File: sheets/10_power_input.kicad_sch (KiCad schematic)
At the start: 8 parts, among them Q1 BUK9M35-80EX, U2 LM74700

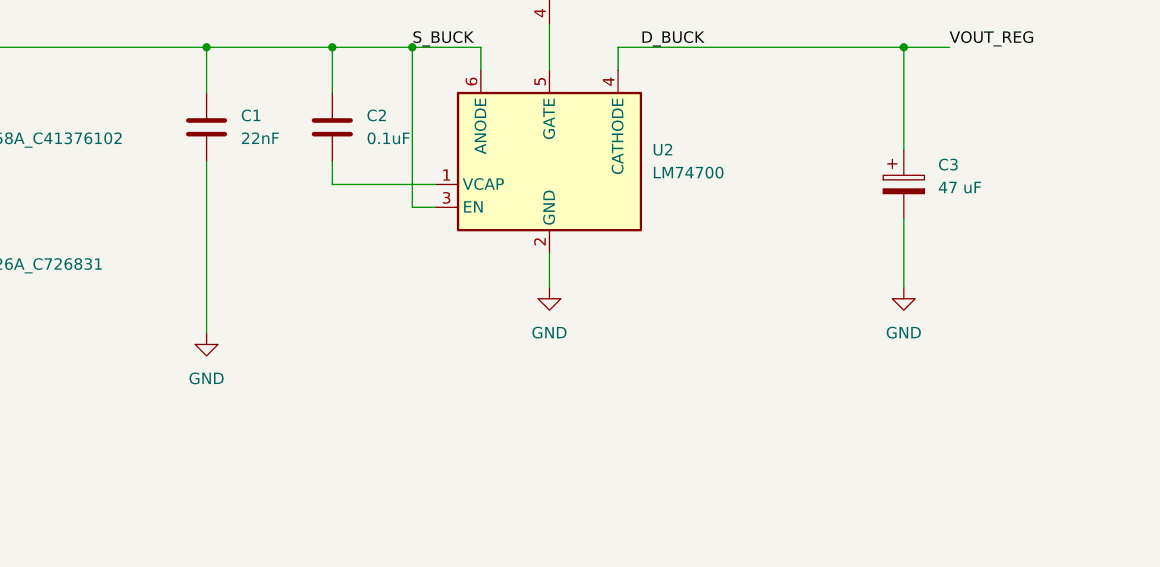
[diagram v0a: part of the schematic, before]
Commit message: Corrige la base del esquemático y añade reglas de proyecto
- Extrae el símbolo ADM3055E a lib/antmicro_adm3055ebriz.kicad_sym y lo
  registra en sym-lib-table con ${KIPRJMOD}.
- U1: huella Package_SO:SOIC-20W_7.5x12.8mm_P1.27mm (nota: verificar
  land pattern contra el datasheet).
- 10_power_input: power:GND -> GND_VEH; huellas y MPN de C1, C2 (0805
  X7R 100 V automotriz), C3 (EEE-HA2A470UP, 10x10) y F1 (1812, MPN
  pendiente).
- Nuevos pines jerárquicos CAN_SILENT (40_mcu -> 60_can, pull-down R1
  10k a GND_ISO) e IMU_INT2 (50_sensors -> 40_mcu).
- CLAUDE.md con reglas de librerías, campos, conexiones entre hojas,
  verificación por hoja y versión prototipo.
- Ignora output/ (reportes generados por kicad-mcp).

Co-Authored-By: Claude Opus 5.5 <noreply@anthropic.com>
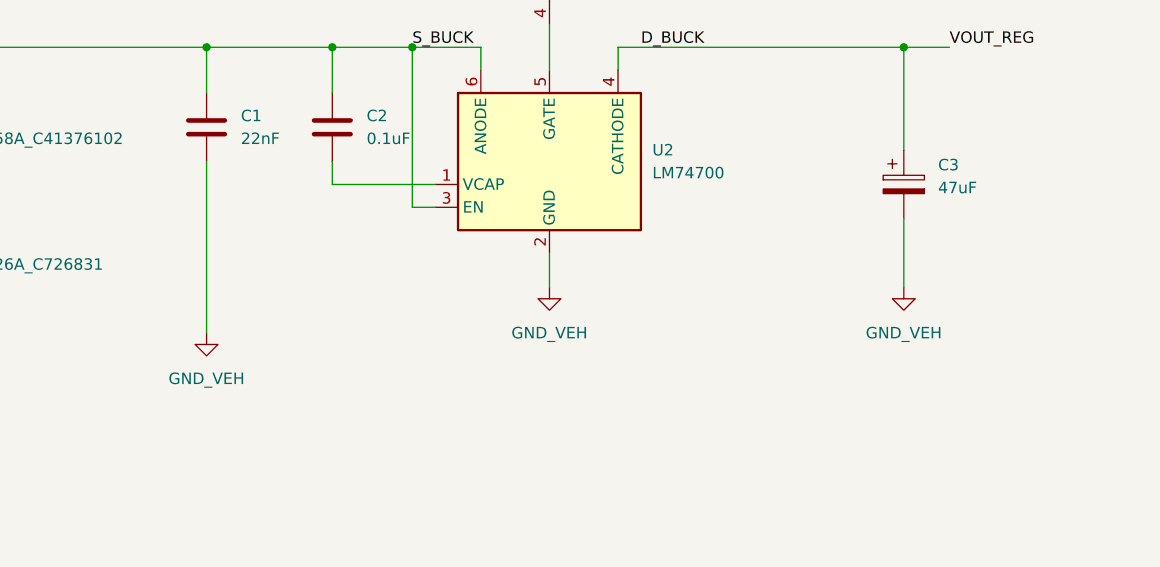
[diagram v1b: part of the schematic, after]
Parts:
- C1: footprint (none) -> Capacitor_SMD:C_0805_2012Metric; MPN (none) -> GCM21BR72A223KA37L; Manufacturer (none) -> Murata; Notes (none) -> 0805 en vez de 0603: lado vehicular (transitorios hasta ~94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; Rating (none) -> 100V X7R 0805 AEC-Q200
- C2: footprint (none) -> Capacitor_SMD:C_0805_2012Metric; MPN (none) -> CGA4J2X7R2A104K125AA; Manufacturer (none) -> TDK; Notes (none) -> 0805 en vez de 0603: lado vehicular (transitorios hasta ~94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; Rating (none) -> 100V X7R 0805 AEC-Q200
- C3: value 47 uF -> 47uF; footprint (none) -> Capacitor_SMD:CP_Elec_10x10; LCSC (none) -> C344077; MPN (none) -> EEE-HA2A470UP; Manufacturer (none) -> Panasonic; Rating (none) -> 100V 105C AEC-Q200 10x10.2
- F1: footprint (none) -> Fuse:Fuse_1812_4532Metric; MPN (none) -> TBD (I_hold pendiente); Manufacturer (none) -> TBD
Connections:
- net GND is gone; now on net GND_VEH: C1.2, C3.2, U2.2 (GND)
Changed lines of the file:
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@@
 			)
 		)
-		(property "Footprint" ""
+		(property "Footprint" "Capacitor_SMD:C_0805_2012Metric"
 			(at 202.8952 133.35 0)
 			(hide yes)
@@
 			)
 		)
-		(property "Datasheet" ""
+		(property "Datasheet" "https://product.tdk.com/en/search/capacitor/ceramic/mlcc/info?part_no=CGA4J2X7R2A104K125AA"
 			(at 201.93 129.54 0)
 			(hide yes)
@@
 		)
 		(property "Description" "Unpolarized capacitor"
+			(at 201.93 129.54 0)
+			(hide yes)
+			(show_name no)
+			(do_not_autoplace no)
+			(effects
+				(font
+					(size 1.27 1.27)
+				)
+			)
+		)
+		(property "MPN" "CGA4J2X7R2A104K125AA"
+			(at 201.93 129.54 0)
+			(hide yes)
+			(show_name no)
+			(do_not_autoplace no)
+			(effects
+				(font
+					(size 1.27 1.27)
+				)
+			)
+		)
+		(property "Manufacturer" "TDK"
+			(at 201.93 129.54 0)
+			(hide yes)
+			(show_name no)
+			(do_not_autoplace no)
+			(effects
+				(font
+					(size 1.27 1.27)
+				)
+			)
+		)
+		(property "Alt_MPN" ""
+			(at 201.93 129.54 0)
+			(hide yes)
+			(show_name no)
+			(do_not_autoplace no)
+			(effects
+				(font
+					(size 1.27 1.27)
+				)
+			)
+		)
+		(property "Rating" "100V X7R 0805 AEC-Q200"
+			(at 201.93 129.54 0)
+			(hide yes)
+			(show_name no)
+			(do_not_autoplace no)
+			(effects
+				(font
+					(size 1.27 1.27)
+				)
+			)
+		)
+		(property "Notes" "0805 en vez de 0603: lado vehicular (transitorios hasta ~94 V tras D1), menor perdida por DC bias que 0603 a 100 V y mas robusto a flexion cerca del conector"
 			(at 201.93 129.54 0)
 			(hide yes)
@@
 			)
 		)
-		(property "Footprint" ""
+		(property "Footprint" "Capacitor_SMD:C_0805_2012Metric"
 			(at 188.9252 133.35 0)
 			(hide yes)
@@
 			)
 		)
-		(property "Datasheet" ""
+		(property "Datasheet" "https://www.murata.com/en-us/products/productdetail?partno=GCM21BR72A223KA37%23"
 			(at 187.96 129.54 0)
 			(hide yes)
@@
 		)
 		(property "Description" "Unpolarized capacitor"
+			(at 187.96 129.54 0)
+			(hide yes)
+			(show_name no)
+			(do_not_autoplace no)
+			(effects
+				(font
+					(size 1.27 1.27)
+				)
+			)
+		)
+		(property "MPN" "GCM21BR72A223KA37L"
+			(at 187.96 129.54 0)
+			(hide yes)
+			(show_name no)
+			(do_not_autoplace no)
+			(effects
+				(font
+					(size 1.27 1.27)
+				)
+			)
+		)
+		(property "Manufacturer" "Murata"
+			(at 187.96 129.54 0)
+			(hide yes)
+			(show_name no)
+			(do_not_autoplace no)
+			(effects
+				(font
+					(size 1.27 1.27)
+				)
+			)
+		)
+		(property "Alt_MPN" ""
+			(at 187.96 129.54 0)
+			(hide yes)
+			(show_name no)
+			(do_not_autoplace no)
+			(effects
+				(font
+					(size 1.27 1.27)
+				)
+			)
+		)
+		(property "Rating" "100V X7R 0805 AEC-Q200"
+			(at 187.96 129.54 0)
+			(hide yes)
+			(show_name no)
+			(do_not_autoplace no)
+			(effects
+				(font
+					(size 1.27 1.27)
+				)
+			)
+		)
+		(property "Notes" "0805 en vez de 0603: lado vehicular (transitorios hasta ~94 V tras D1), menor perdida por DC bias que 0603 a 100 V y mas robusto a flexion cerca del conector"
 			(at 187.96 129.54 0)
 			(hide yes)
@@
 	)
 	(symbol
-		(lib_id "power:GND")
+		(lib_id "INCLI-VA:GND_VEH")
 		(at 226.06 147.32 0)
 		(unit 1)
@@
 			)
 		)
-		(property "Value" "GND"
+		(property "Value" "GND_VEH"
 			(at 226.06 152.4 0)
 			(show_name no)
@@
 			)
 		)
-		(property "Value" "47 uF"
+		(property "Value" "47uF"
 			(at 269.24 136.2709 0)
 			(show_name no)
@@
 			)
 		)
-		(property "Footprint" ""
+		(property "Footprint" "Capacitor_SMD:CP_Elec_10x10"
 			(at 266.3952 139.7 0)
 			(hide yes)
@@
 			)
 		)
-		(property "Datasheet" ""
+		(property "Datasheet" "https://industrial.panasonic.com/ww/products/pt/aluminum-cap-smd/models/EEEHA2A470UP"
 			(at 265.43 135.89 0)
 			(hide yes)
@@
 		)
 		(property "Description" "Polarized capacitor"
+			(at 265.43 135.89 0)
+			(hide yes)
+			(show_name no)
+			(do_not_autoplace no)
+			(effects
+				(font
+					(size 1.27 1.27)
+				)
+			)
+		)
+		(property "MPN" "EEE-HA2A470UP"
+			(at 265.43 135.89 0)
+			(hide yes)
+			(show_name no)
+			(do_not_autoplace no)
+			(effects
+				(font
+					(size 1.27 1.27)
+				)
+			)
+		)
+		(property "Manufacturer" "Panasonic"
+			(at 265.43 135.89 0)
+			(hide yes)
+			(show_name no)
+			(do_not_autoplace no)
+			(effects
+				(font
+					(size 1.27 1.27)
+				)
+			)
+		)
+		(property "LCSC" "C344077"
+			(at 265.43 135.89 0)
+			(hide yes)
+			(show_name no)
+			(do_not_autoplace no)
+			(effects
+				(font
+					(size 1.27 1.27)
+				)
+			)
+		)
+		(property "Alt_MPN" ""
+			(at 265.43 135.89 0)
+			(hide yes)
+			(show_name no)
+			(do_not_autoplace no)
+			(effects
+				(font
+					(size 1.27 1.27)
+				)
+			)
+		)
+		(property "Rating" "100V 105C AEC-Q200 10x10.2"
 			(at 265.43 135.89 0)
 			(hide yes)
@@
 	)
 	(symbol
-		(lib_id "power:GND")
+		(lib_id "INCLI-VA:GND_VEH")
 		(at 187.96 152.4 0)
 		(unit 1)
@@
 			)
 		)
-		(property "Value" "GND"
+		(property "Value" "GND_VEH"
 			(at 187.96 157.48 0)
 			(show_name no)
@@
 	)
 	(symbol
-		(lib_id "power:GND")
+		(lib_id "INCLI-VA:GND_VEH")
 		(at 265.43 147.32 0)
 		(unit 1)
@@
 			)
 		)
-		(property "Value" "GND"
+		(property "Value" "GND_VEH"
 			(at 265.43 152.4 0)
 			(show_name no)
@@
 			)
 		)
-		(property "Footprint" ""
+		(property "Footprint" "Fuse:Fuse_1812_4532Metric"
 			(at 152.4 119.38 0)
 			(hide yes)
@@
 			(at 147.32 120.65 0)
 			(hide yes)
+			(show_name no)
+			(do_not_autoplace no)
+			(effects
+				(font
+					(size 1.27 1.27)
+				)
+			)
+		)
+		(property "MPN" "TBD (I_hold pendiente)"
+			(at 147.32 120.65 0)
+			(hide yes)
+			(show_name no)
+			(do_not_autoplace no)
+			(effects
+				(font
+					(size 1.27 1.27)
+				)
+			)
+		)
+		(property "Manufacturer" "TBD"
+			(at 147.32 120.65 0)
+			(hide yes)
+			(show_name no)
+			(do_not_autoplace no)
+			(effects
+				(font
+					(size 1.27 1.27)
+				)
+			)
+		)
+		(property "Alt_MPN" ""
+			(at 147.32 120.65 0)
+			(hide yes)

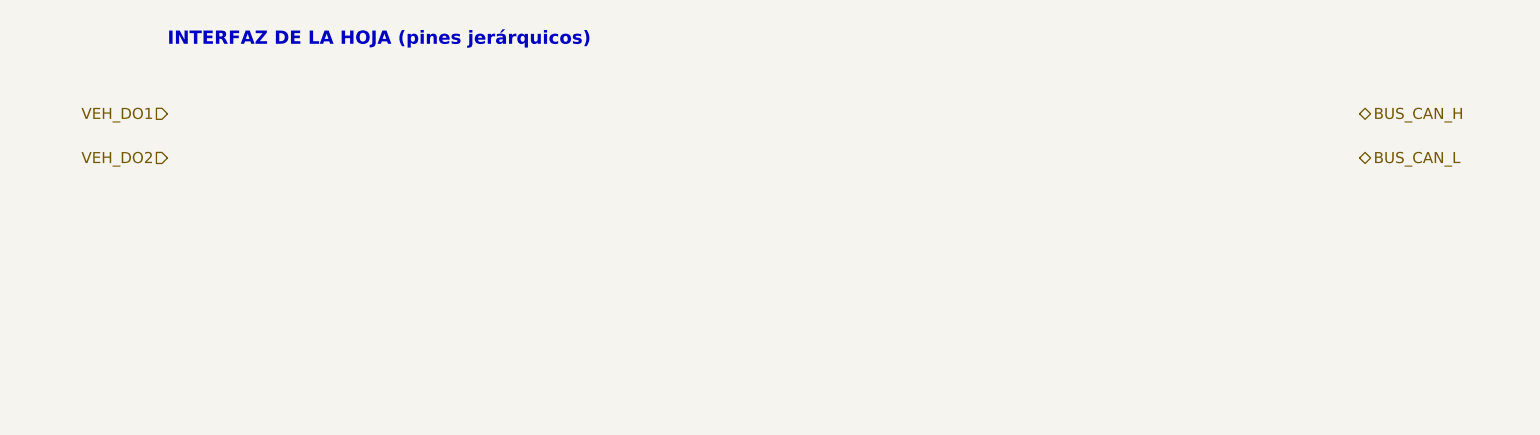
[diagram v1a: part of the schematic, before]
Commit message: 70_output: salida low-side con latch y señal PWR_FLT
- 70_output (DO1/DO2): MOSFET FDD7N25LZ (demo, 250 V) con TVS SMCJ188A
  en el drenador, latch de sobrecorriente a ~0.7 A (R 1 ohm + BC817/BC807,
  rearme con EN=0), apagado del gate por PWR_FLT_N o latch (BAT54A) y
  DIAG por divisor del drenador con zener 5V1. OUT pasa a pasivo.
- Jerarquía: VEH_PWR_FLT_N de 10_power_input a 70_output y 20_isolation;
  PWR_FLT de 20_isolation a 40_mcu (KW45 y ESP32-S3).
- 10_power_input: solo interfaz (VEH_DO1/2 pasivos, VEH_PWR_FLT_N);
  el circuito con LM74930 va en un commit aparte.
- CLAUDE.md: procedimiento para componentes fuera de las librerías.
- README: 70_output es low-side.

Co-Authored-By: Claude Opus 5.5 <noreply@anthropic.com>
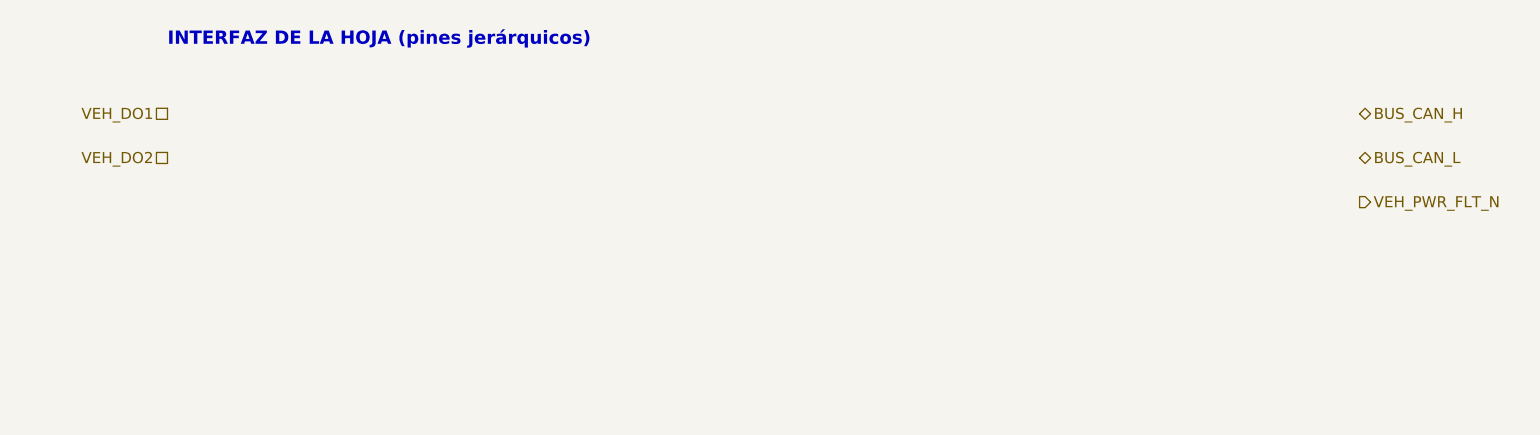
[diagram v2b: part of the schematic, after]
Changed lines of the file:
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@@
 	)
 	(hierarchical_label "VEH_DO1"
-		(shape input)
+		(shape passive)
 		(at 238.76 30.48 180)
 		(effects
@@
 	)
 	(hierarchical_label "VEH_DO2"
-		(shape input)
+		(shape passive)
 		(at 238.76 35.56 180)
 		(effects
@@
 		)
 	)
+	(hierarchical_label "VEH_PWR_FLT_N"
+		(shape output)
+		(at 375.92 40.64 0)
+		(effects
+			(font
+				(size 1.27 1.27)
+			)
+			(justify left)
+		)
+	)

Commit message: 10_power_input: protección de entrada con LM74930-Q1 y conectores
- U101 LM74930-Q1 (ref. TI 8.2, load dump 202 V sin suprimir):
  Q101 STD18NF25 (corte, 250 V) + Q102 IPD30N10S3L-34 (diodo ideal),
  corte por OV a 38.4 V, UVLO ~6.5 V, breaker 1 A (R_SENSE 10 mohm,
  R_ILIM 60.4k), corto 2 A, C_TMR 68 nF, VS con R 10k + SMAJ51A + BAS21.
  FLT -> VEH_PWR_FLT_N. Pad expuesto (RTN) flotante según TI.
- Entrada: F101 2 A/250 VDC (huella 2410 pendiente), D101 ES2G +
  D102 SMCJ33A, C_IN 450 V. Salida: C104 47 uF, hold-up C105 DNP,
  filtro LC a +VPROT. PWR_FLAG y test points.
- J1 MSTB 5 pines (V+, GND_VEH, CAN_H, CAN_L, CAN_GND) y J2 MSTB 2
  pines (DO1, DO2). Se elimina el circuito anterior con LM74700.
- Librería easyeda2kicad (LCSC C22428070) registrada con ${KIPRJMOD};
  símbolo convertido a formato KiCad 10 y tipos de pin según TI.
- 70_output: Q701 FDD7N25LZ (demo) y D701 SMCJ188A, con Notes.

Co-Authored-By: Claude Opus 5.5 <noreply@anthropic.com>
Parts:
- removed C1: 22nF, Capacitor_SMD:C_0805_2012Metric, symbol Device:C
- removed C2: 0.1uF, Capacitor_SMD:C_0805_2012Metric, symbol Device:C
- removed C3: 47uF, Capacitor_SMD:CP_Elec_10x10, symbol Device:C_Polarized
- removed D1: SMBJ58A_C41376102, INCLI-VA:SMB_L4.6-W3.6-LS5.3-R-RD, symbol INCLI-VA:SMBJ58A_C41376102
- removed D2: SMBJ26A_C726831, INCLI-VA:SMB_L4.4-W3.6-LS5.3-RD, symbol INCLI-VA:SMBJ26A_C726831
- removed F1: Polyfuse, Fuse:Fuse_1812_4532Metric, symbol Device:Polyfuse
- removed Q1: BUK9M35-80EX, Package_TO_SOT_SMD:LFPAK33, symbol Transistor_FET:BUK9M35-80EX
- removed U2: LM74700, Package_TO_SOT_SMD:SOT-23-6, symbol Power_Management:LM74700
- added C101: 100nF, Capacitor_SMD:C_1206_3216Metric, symbol Device:C
- added C102, C103: 1uF, Capacitor_SMD:C_1206_3216Metric, symbol Device:C
- added C104: 47uF, Capacitor_SMD:CP_Elec_10x10, symbol Device:C_Polarized
- added C105: 1000uF DNP, Capacitor_SMD:CP_Elec_16x17.5, symbol Device:C_Polarized
- added C106: 10uF, Capacitor_SMD:C_1210_3225Metric, symbol Device:C
- added C107, C108: 100nF, Capacitor_SMD:C_0603_1608Metric, symbol Device:C
- added C109: 10nF, Capacitor_SMD:C_0603_1608Metric, symbol Device:C
- added C110: 68nF, Capacitor_SMD:C_0603_1608Metric, symbol Device:C
- added D101: ES2G, Diode_SMD:D_SMB, symbol Device:D
- added D102: SMCJ33A, Diode_SMD:D_SMC, symbol Diode:SM6T33A
- added D103: SMAJ51A, Diode_SMD:D_SMA, symbol Diode:SM6T56A
- added D104: BAS21, Package_TO_SOT_SMD:SOT-23, symbol Diode:BAS21
- added F101: 2A 250VDC, symbol Device:Fuse
- added J1: MSTB 2,5/5-GF-5,08, Connector_Phoenix_MSTB:PhoenixContact_MSTB_2,5_5-GF-5,08_1x05_P5.08mm_Horizontal_ThreadedFlange, symbol Connector_Generic:Conn_01x05
- added J2: MSTB 2,5/2-GF-5,08, Connector_Phoenix_MSTB:PhoenixContact_MSTB_2,5_2-GF-5,08_1x02_P5.08mm_Horizontal_ThreadedFlange, symbol Connector_Generic:Conn_01x02
- added L101: 10uH, Inductor_SMD:L_Bourns_SRN6045TA, symbol Device:L
- added Q101: STD18NF25, Package_TO_SOT_SMD:TO-252-2, symbol Transistor_FET:IPD50R380CE
- added Q102: IPD30N10S3L-34, Package_TO_SOT_SMD:TO-252-2, symbol Transistor_FET:IPD50R380CE
- added R102: 10k, Resistor_SMD:R_2512_6332Metric, symbol Device:R
- added R103: 10m, Resistor_SMD:R_1206_3216Metric, symbol Device:R
- added R104: 49.9, Resistor_SMD:R_0603_1608Metric, symbol Device:R
- added R105: 100, Resistor_SMD:R_0603_1608Metric, symbol Device:R
- added R106: 100k, Resistor_SMD:R_0603_1608Metric, symbol Device:R
- added R107: 9.31k, Resistor_SMD:R_0603_1608Metric, symbol Device:R
- added R108, R112: 51k, Resistor_SMD:R_1206_3216Metric, symbol Device:R
- added R109: 1.62k, Resistor_SMD:R_0603_1608Metric, symbol Device:R
- added R110: 60.4k, Resistor_SMD:R_0603_1608Metric, symbol Device:R
- added R111: 10k, Resistor_SMD:R_0603_1608Metric, symbol Device:R
- added TP101: +VPROT, TestPoint:TestPoint_Pad_D1.5mm, symbol Connector:TestPoint
- added TP102: VBAT_F, TestPoint:TestPoint_Pad_D1.5mm, symbol Connector:TestPoint
- added TP103: GND_VEH, TestPoint:TestPoint_Pad_D1.5mm, symbol Connector:TestPoint
- added TP104: FLT, TestPoint:TestPoint_Pad_D1.5mm, symbol Connector:TestPoint
- added U101: LM74930QRGERQ1, easyeda2kicad:VQFN-24_L4.0-W4.0-P0.50-TL-EP2.1, symbol easyeda2kicad:LM74930QRGERQ1
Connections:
- net +VPROT: now also C106.1, C107.1, L101.2, TP101.1
- net BUS_CAN_H: now also J1.3 (Pin_3)
- net BUS_CAN_L: now also J1.4 (Pin_4)
- net GND_CAN: now also J1.5 (Pin_5)
- net GND_VEH: now also C101.2, C102.2, C103.2, C104.2, C105.2, C106.2, C107.2, C109.2, C110.2, D102.1 (A1), D103.2 (A2), J1.2 (Pin_2), R107.2, R109.2, R110.2, TP103.1, U101.13 (GND), U101.16 (OVCLAMP)
- net VEH_DO1: now also J2.1 (Pin_1)
- net VEH_DO2: now also J2.2 (Pin_2)
- net VEH_PWR_FLT_N: now also R111.2, TP104.1, U101.12 (FLT)
- net VIN_VEH: now also F101.1, J1.1 (Pin_1)
- new net: D101.2 (A), D102.2 (A2)
- new net: C109.1, R105.2
- new net: D103.1 (A1), D104.1 (A), R102.2
- new net: R108.2, R112.1
- new net +5V_VEH: R111.1
- new net CAP: C108.1, U101.23 (CAP)
- new net CSP: R104.1, U101.20 (CS+)
- new net C_ID: C103.1, Q102.2 (D), R103.1, R104.2, U101.18 (ISCP), U101.24 (C)
- new net DGATE: Q102.1 (G), U101.1 (DGATE)
- new net HGATE: Q101.1 (G), R105.1, U101.14 (HGATE)
- new net ILIM: R110.1, U101.11 (ILIM)
- new net OV: R109.1, R112.2, U101.5 (OV)
- new net SW: R106.1, U101.3 (SW)
- new net TMR: C110.1, U101.9 (TMR)
- new net UVLO: R106.2, R107.1, U101.4 (UVLO)
- new net VA: Q101.3 (S), Q102.3 (S), U101.15 (OUT), U101.2 (A)
- new net VBAT_F: C101.1, D101.1 (K), F101.2, Q101.2 (D), R102.1, R108.1, TP102.1
- new net VOUT: C104.1, C105.1, L101.1, R103.2, U101.19 (CS-)
- new net VS: C102.1, C108.2, D104.3 (K), U101.22 (VS), U101.6 (EN), U101.7 (MODE)
- no-connect marks 0 -> 1
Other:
- note added: "BLOQUE 10 — ENTRADA DE ALIMENTACIÓN, CONECTORES [dominio VEH] (común a KW45 y ESP32-S3) J1 (MSTB 5 pines): V+, GND_VEH, CAN_H, CAN_L, CAN_GND. J2 (MSTB 2 pines): DO1, DO2 (low-side de 70_output; su protección va junto a J2). F101 fusible 2 A / 250 VDC, solo para fallas graves (el breaker del LM74930 actúa antes, a 1 A). D101 ES2G + D102 SMCJ33A: TVS- para ISO 7637-2 pulso 1 (-600 V) y bloqueo en 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"
- note added: "RIELES USADOS EN ESTA HOJA: GND_VEH, GND_CAN, +VPROT (sale), +5V_VEH (pull-up de FLT)"
- note removed: "BLOQUE 10 — ENTRADA DE ALIMENTACIÓN [dominio VEH] (común a KW45 y ESP32-S3) Cadena: VIN 9-36 V → PTC → LM74700-Q1 + MOSFET N → TVS → filtro LC = +VPROT Componentes: J1 Conector M12 8 pines código A, montaje en panel F1 Fusible PTC reseteable (sobrecorriente de entrada) U1 TI LM74700-Q1 + Q1 MOSFET N (diodo ideal, polaridad inversa) D1 TVS SM8S (o SMBJ según ensayo) — load dump 24 V L1, C Filtro L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"
- note removed: "INTERFAZ DE LA HOJA (pines jerárquicos)"
- note removed: "RIELES USADOS EN ESTA HOJA"

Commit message: U101: huella VQFN-24 corregida en INCLI-VA.pretty
- Nueva huella TI_RGE0024T_..._HandSolder_IsolatedVias a partir del land
  pattern de TI (RGE0024T): paso exacto de 0.5 mm, pads de 0.85 mm (mismo
  borde interior que TI, más largos para soldar a mano), pasta del EP en
  4 x 0.94 mm, 5 vías de 0.2 mm hacia una isla aislada en B.Cu (el EP es
  RTN y debe quedar flotante), courtyard de +-2.7 mm y modelo 3D con
  ${KIPRJMOD}/lib/INCLI-VA.3dshapes.
- U101 y el símbolo LM74930QRGERQ1 apuntan a la huella nueva.
- CLAUDE.md: excepción para crear huellas de pasivos de 2 terminales
  desde el datasheet en INCLI-VA.pretty.

Co-Authored-By: Claude Opus 5.5 <noreply@anthropic.com>
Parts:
- U101: footprint easyeda2kicad:VQFN-24_L4.0-W4.0-P0.50-TL-EP2.1 -> INCLI-VA:TI_RGE0024T_VQFN-24-1EP_4x4mm_P0.5mm_EP2.1mm_HandSolder_IsolatedVias; Notes VQFN-24 aceptado para el demo. Pad expuesto = RTN: dejar FLOTANTE (TI), no conectar a GND. Huella importada con diferencias vs RGE0024T: ver conversación de diseño. LCSC C22428070. -> VQFN-24 aceptado para el demo. Pad expuesto = RTN: dejar FLOTANTE (TI), no conectar a GND. Huella INCLI-VA (corregida desde RGE0024T): paso exacto, pasta 4x0.94 mm, 5 vías a isla aislada en B.Cu (RTN), courtyard +-2.7 mm. LCSC C22428070.
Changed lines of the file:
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@@
 			)
 		)
-		(property "Footprint" "easyeda2kicad:VQFN-24_L4.0-W4.0-P0.50-TL-EP2.1"
+		(property "Footprint" "INCLI-VA:TI_RGE0024T_VQFN-24-1EP_4x4mm_P0.5mm_EP2.1mm_HandSolder_IsolatedVias"
 			(at 134.62 106.68 0)
 			(hide yes)
@@
 			)
 		)
-		(property "Notes" "VQFN-24 aceptado para el demo. Pad expuesto = RTN: dejar FLOTANTE (TI), no conectar a GND. Huella importada con diferencias vs RGE0024T: ver conversación de diseño. LCSC C22428070."
+		(property "Notes" "VQFN-24 aceptado para el demo. Pad expuesto = RTN: dejar FLOTANTE (TI), no conectar a GND. Huella INCLI-VA (corregida desde RGE0024T): paso exacto, pasta 4x0.94 mm, 5 vías a isla aislada en B.Cu (RTN), courtyard +-2.7 mm. LCSC C22428070."
 			(at 134.62 106.68 0)
 			(hide yes)
